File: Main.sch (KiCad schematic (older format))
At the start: 63 parts

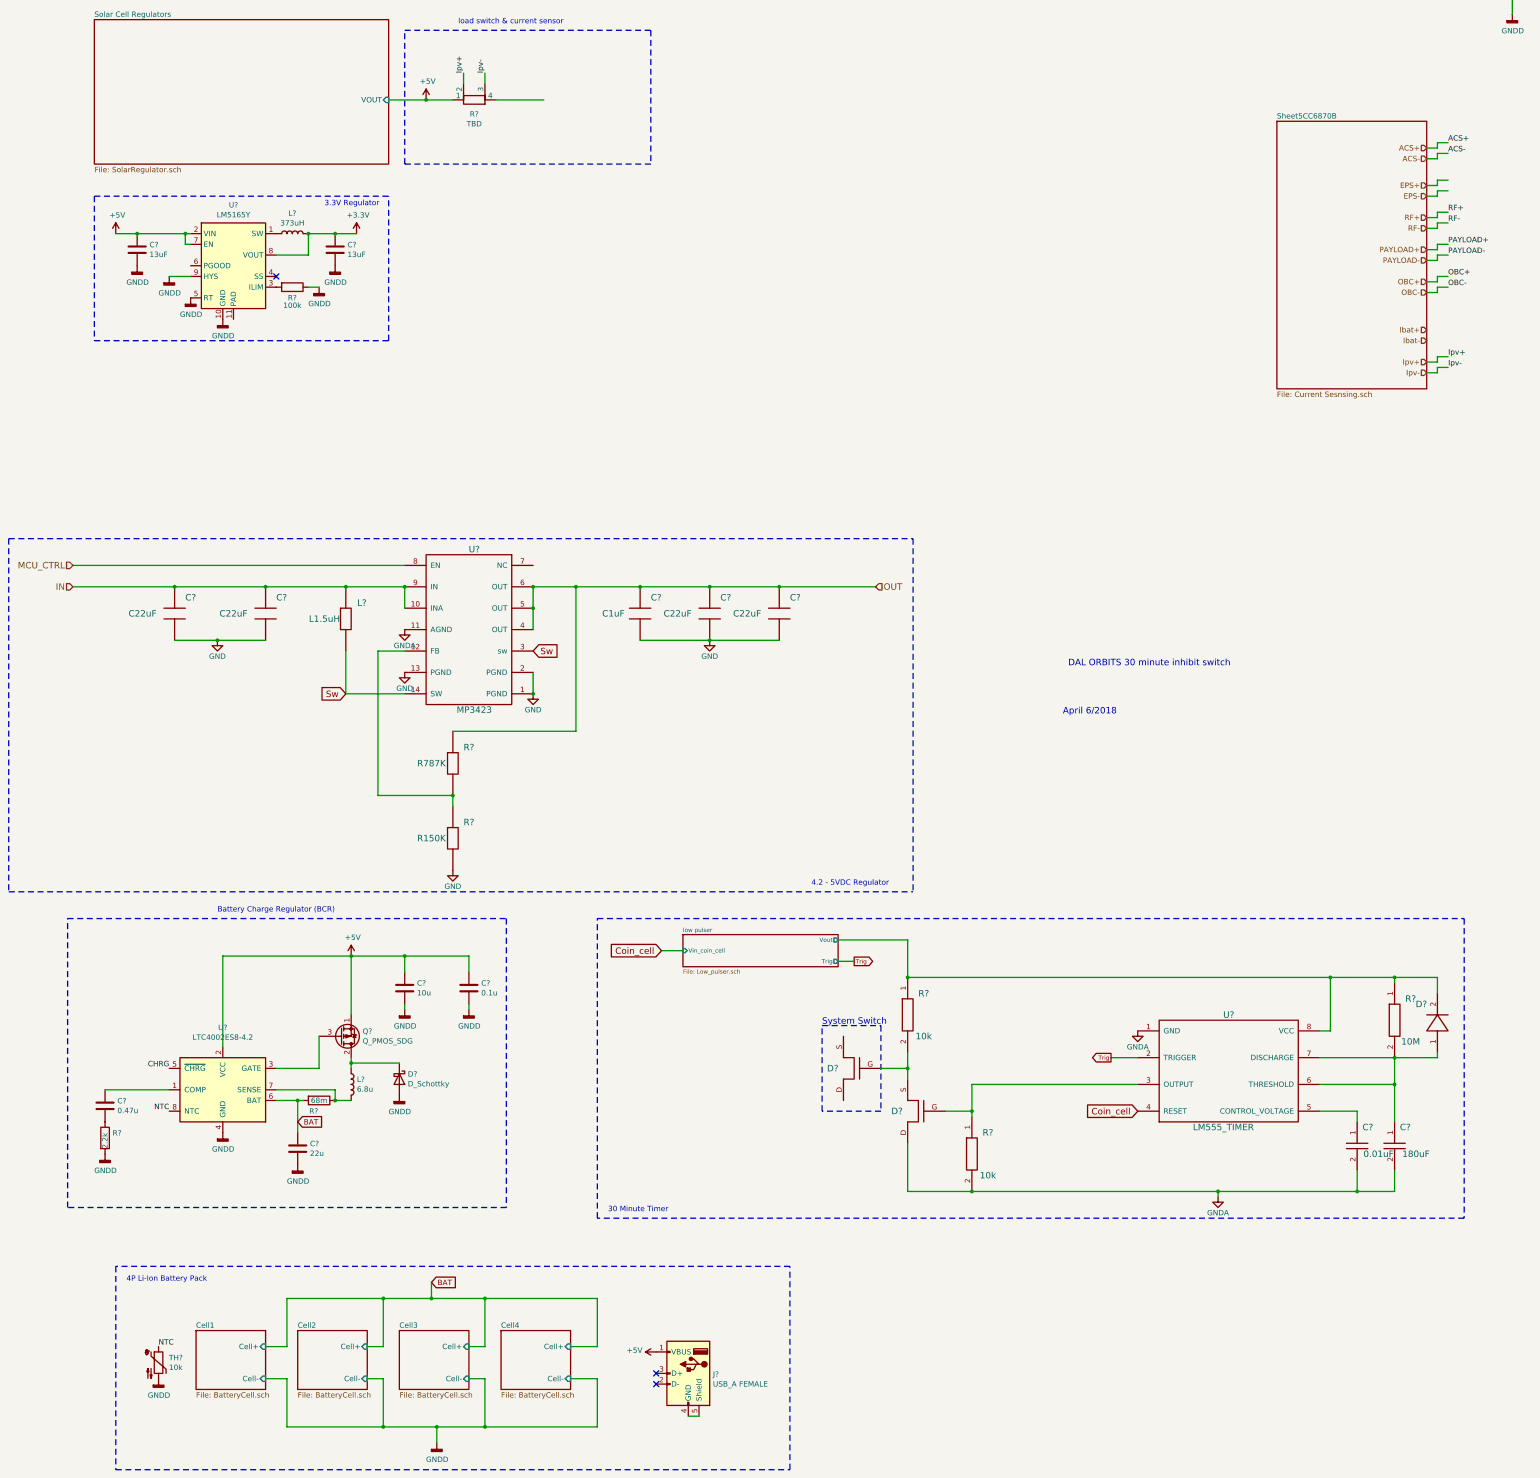
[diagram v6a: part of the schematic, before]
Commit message: added system switch to negative terminal of battery pack. moved BDR and BCR to hierarchical sheets for improved readability
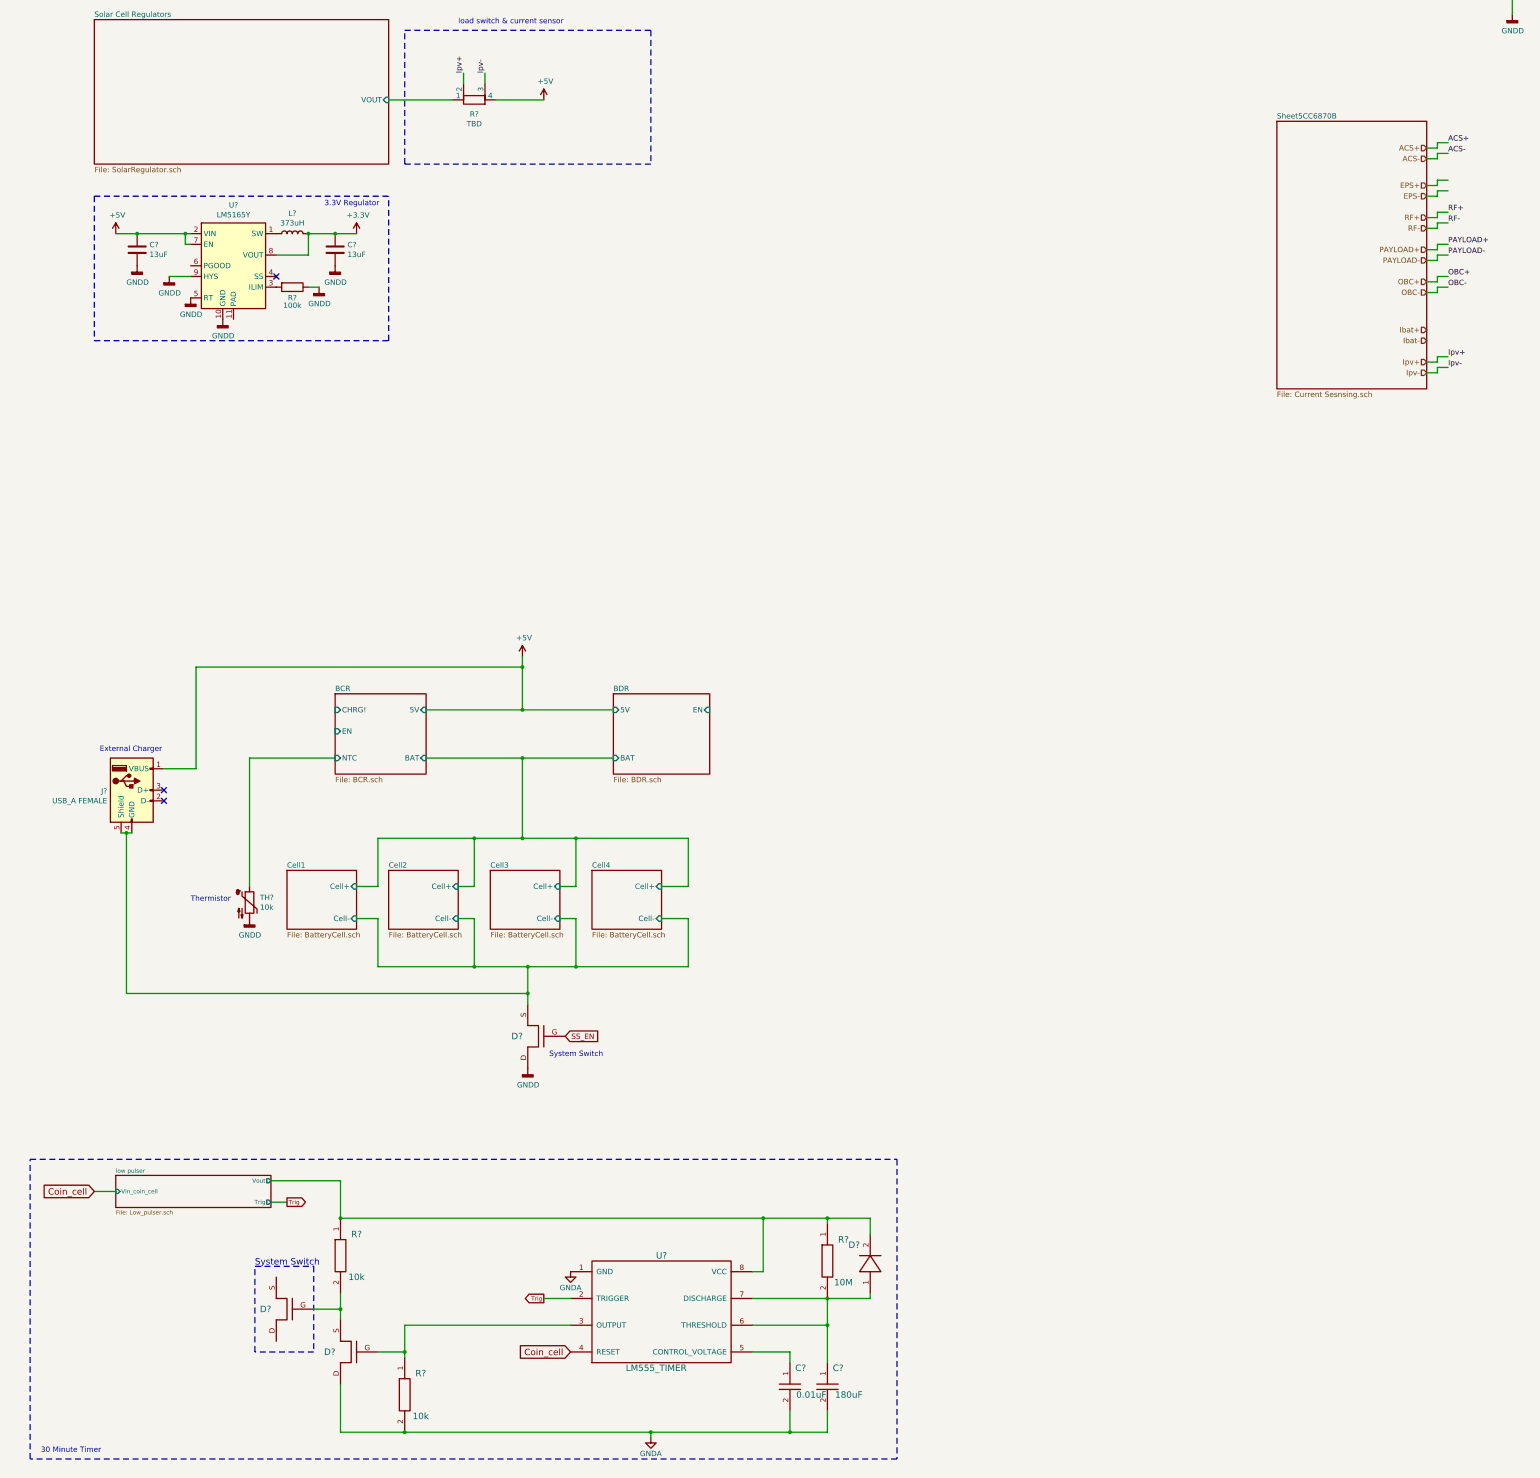
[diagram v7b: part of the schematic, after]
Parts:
- removed C?: 22u, symbol Device:C
- removed C?: 0.47u, symbol Device:C
- removed C?: 10u, symbol Device:C
- removed C?: 0.1u, symbol Device:C
- removed C?: C1uF, symbol 4.2-5V_regulator:C1uF
- removed C? (x4): C22uF, symbol 4.2-5V_regulator:C22uF
- removed D?: D_Schottky, symbol Device:D_Schottky
- removed L?: 6.8u, symbol Device:L
- removed L?: L1.5uH, symbol 4.2-5V_regulator:L1.5uH
- removed Q?: Q_PMOS_SDG, symbol Device:Q_PMOS_SDG
- removed R?: 68m, symbol Device:R
- removed R?: 2.2k, symbol Device:R
- removed R?: R150K, symbol 4.2-5V_regulator:R150K
- removed R?: R787K, symbol 4.2-5V_regulator:R787K
- removed U?: MP3423, symbol 4.2-5V_regulator:MP3423
- removed U?: LTC4002ES8-4.2, Package_SO:SOIC-8_3.9x4.9mm_P1.27mm, symbol Battery_Management:LTC4002ES8-4.2
- added D?: FET(reversed), symbol Main-rescue:FET(reversed)-555_timer-rescue
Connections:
- net labels added: SS_EN
- net labels removed: BAT, CHRG, GND, IN, MCU_CTRL, NTC, OUT, Sw
- wire segments 214 -> 181
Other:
- note added: "External Charger"
- note added: "Thermistor"
- note removed: "4.2 - 5VDC Regulator"
- note removed: "4P Li-Ion Battery Pack"
- note removed: "April 6/2018"
- note removed: "Battery Charge Regulator (BCR)"
- note removed: "DAL ORBITS 30 minute inhibit switch"
- moved on the sheet: C?, D?, J?, R?, TH?, U?

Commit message: Added more hierarchical sheets to improve readability, restructured the main schematic, and added ideal diode betewen BCR and BDR
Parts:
- removed C? (x2): 13uF, symbol Device:C
- removed L?: 373uH, symbol Device:L
- removed R?: 100k, symbol Device:R
- removed U?: LM5165Y, Package_SON:Texas_S-PVSON-N10_ThermalVias, symbol Regulator_Switching:LM5165Y
- added D?: Diode, symbol 555timer:Diode
- added D?: FET(reversed), symbol Main-rescue:FET(reversed)-555_timer-rescue
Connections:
- wire segments 181 -> 177
- no-connect marks 13 -> 12
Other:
- note removed: "3.3V Regulator"
- note removed: "Power Distribution Unit (PDU)"
- note removed: "load switch & current sensor"
- moved on the sheet: C?, D?, J?, R?, TH?, U?
